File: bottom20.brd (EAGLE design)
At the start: 160 x 140 mm, 142 parts, among them T1:IC1 MULTIPLEXER, T1:R1 20k, T1:R10 20k, T1:R11 20k, T1:R12 20k, T1:R13 20k, T1:R14 20k, T1:R15 20k, T1:R16 20k, T1:R17 10k, T1:R2 20k, T1:R3 20k, T1:R4 20k, T1:R5 20k, T1:R6 20k, T1:R7 20k, T1:R8 20k, T1:R9 20k, T1:T1 SFH320, T1:T10 SFH320, T1:T11 SFH320, T1:T12 SFH320, T1:T13 SFH320, T1:T14 SFH320, T1:T15 SFH320, T1:T16 SFH320, T1:T2 SFH320, T1:T3 SFH320, T1:T4 SFH320, T1:T5 SFH320, T1:T6 SFH320, T1:T7 SFH320, T1:T8 SFH320, T1:T9 SFH320, T2:IC1 MULTIPLEXER, T2:R1 20k, T2:R10 20k, T2:R11 20k, T2:R12 20k, T2:R13 20k, T2:R14 20k, T2:R15 20k, T2:R16 20k, T2:R17 10k, T2:R2 20k, T2:R3 20k, T2:R4 20k, T2:R5 20k, T2:R6 20k, T2:R7 20k, T2:R8 20k, T2:R9 20k, T2:T1 SFH320, T2:T10 SFH320, T2:T11 SFH320, T2:T12 SFH320, T2:T13 SFH320, T2:T14 SFH320, T2:T15 SFH320, T2:T16 SFH320, T2:T2 SFH320, T2:T3 SFH320, T2:T4 SFH320, T2:T5 SFH320, T2:T6 SFH320, T2:T7 SFH320, T2:T8 SFH320, T2:T9 SFH320

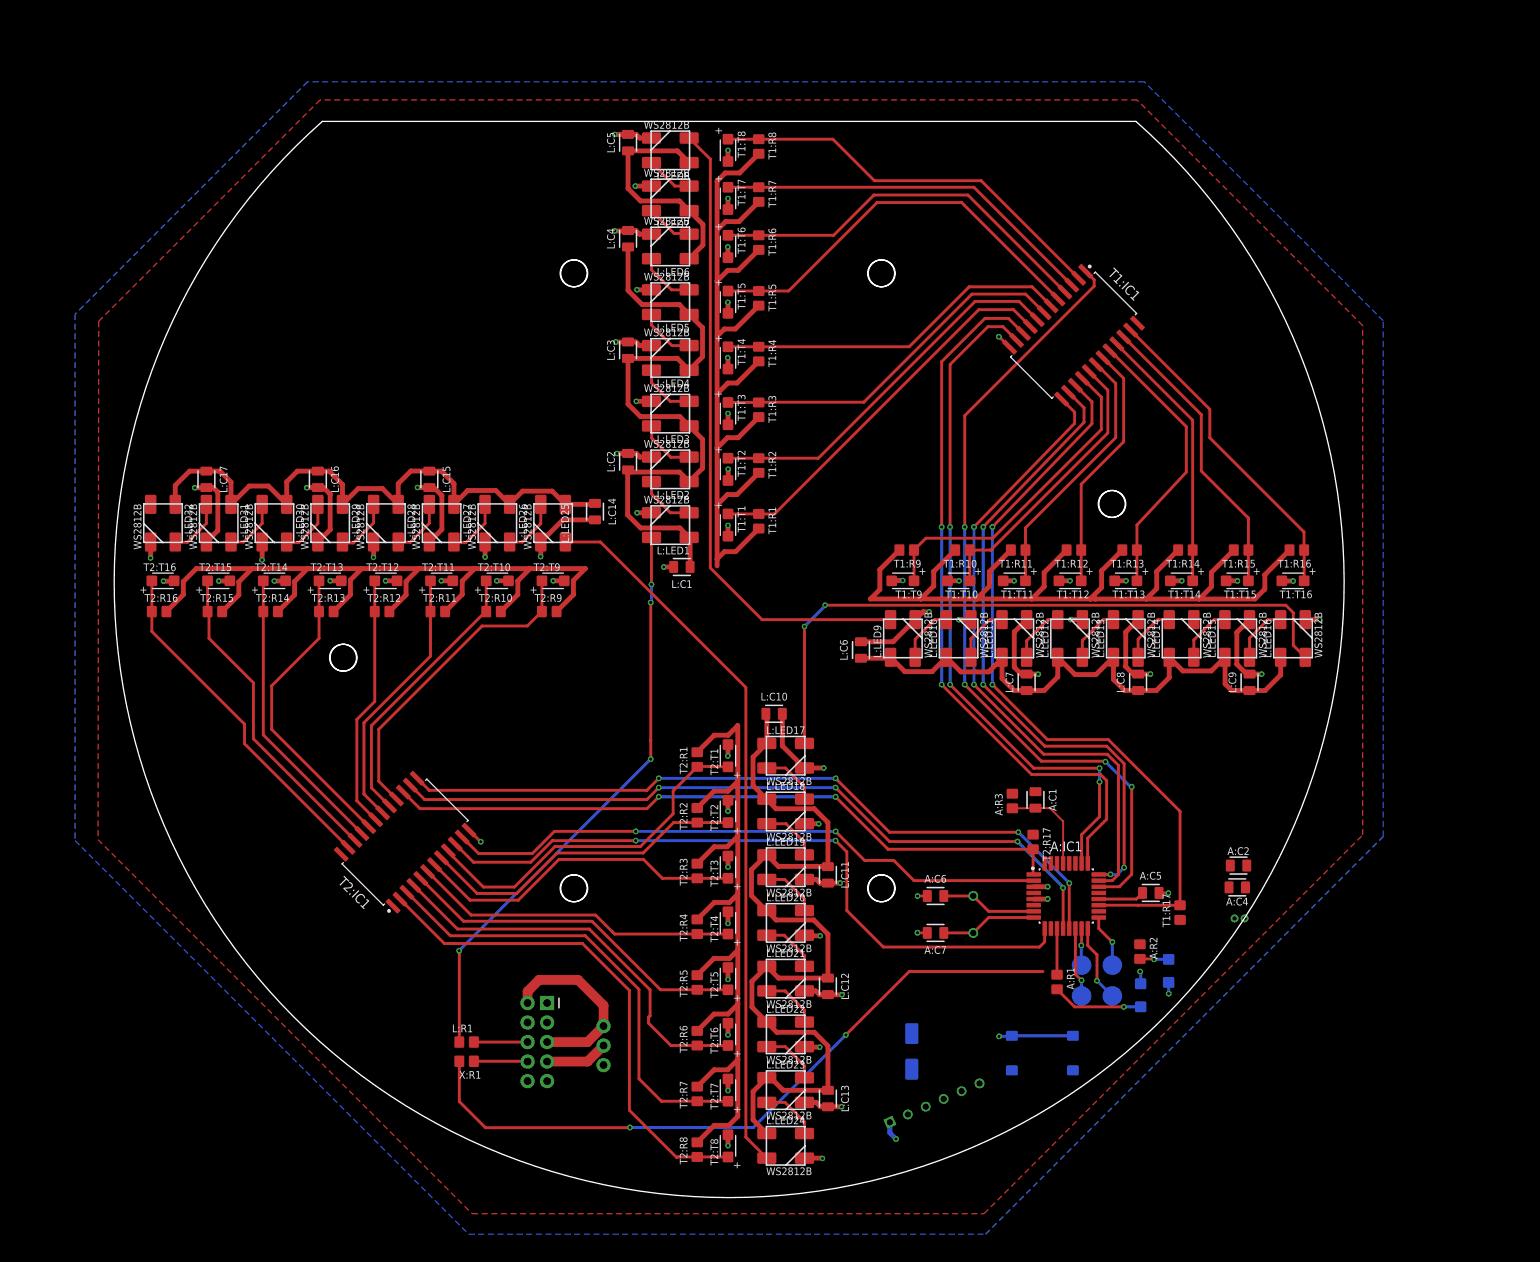
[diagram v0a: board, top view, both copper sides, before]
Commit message: - bot.sch (Routing - only 5V missing)
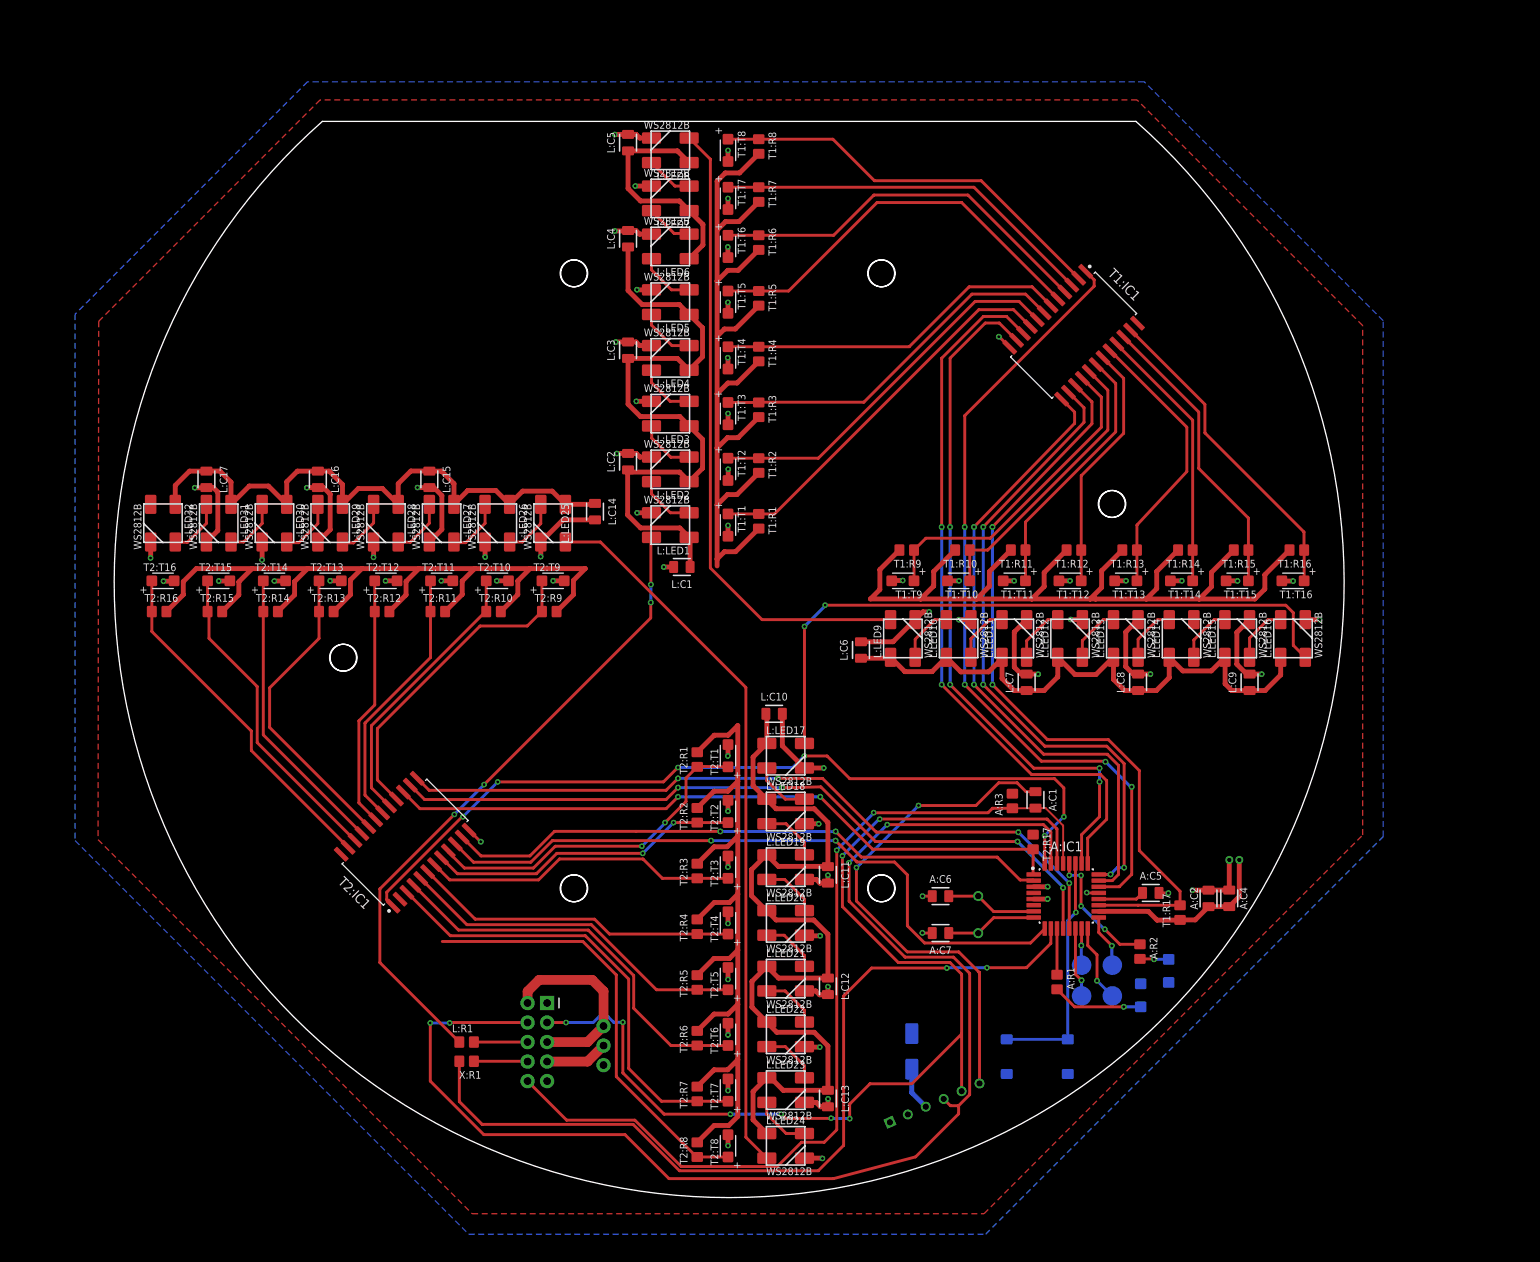
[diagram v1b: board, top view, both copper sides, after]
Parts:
- moved A:C3 7.64 mm to (65.9, -36.3), turned to 0 degrees
- moved A:C2 5.79 mm to (62.5, -41.3), turned to 90 degrees
- moved A:C4 1.77 mm to (65.2, -41.3), turned to 90 degrees
- moved A:S2 0.81 mm to (40.2, -61.9), turned to 180 degrees
- moved A:C7 0.65 mm to (27.6, -45.8)
- moved A:Q1 0.65 mm to (32.5, -43.4)
- moved A:C6 0.65 mm to (27.6, -41.0)
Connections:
- removed net A:ARD-INTERRUPT: A:IC1.10
- removed net X:ARD-INTERRUPT: X:R1.2
- removed net X:ARD-RX: X:X2.3
- removed net X:ARD-TX: X:X2.4
- new net ARD-INTERRUPT: A:IC1.10, X:R1.2
- net RX: now also X:X2.3
- net TX: now also X:X2.4
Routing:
- net TX: track 0.00 -> 175.5 mm, vias 0 -> 4
- net RX: track 0.00 -> 145.4 mm, vias 0 -> 8
- net ARD-INTERRUPT: track 0.00 -> 111.5 mm, vias 0 -> 2
- net N$2: track 0.00 -> 110.2 mm, vias 0 -> 6
- net ARD-RESET: track 12.8 -> 120.9 mm, vias 0 -> 2
- net X:ARD-INTERRUPT: track 91.0 -> 0.00 mm, vias 2 -> 0
- net DTR: track 0.00 -> 67.1 mm, vias 0 -> 2
- net A:N$9: track 0.00 -> 31.3 mm, vias 0 -> 1
- net +5V: track 824.3 -> 848.9 mm
- net A:N$11: track 0.00 -> 16.8 mm, vias 0 -> 4
- net T2:N$9: track 65.8 -> 56.5 mm
- net L:N$10: track 76.0 -> 84.6 mm
- net GND: track 241.3 -> 234.3 mm, vias 75 -> 73
- net X:VID: track 0.00 -> 5.64 mm
- net T2:N$2: track 43.0 -> 40.9 mm, vias 0 -> 2
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
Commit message: - bot.sch (Routing - corrections)
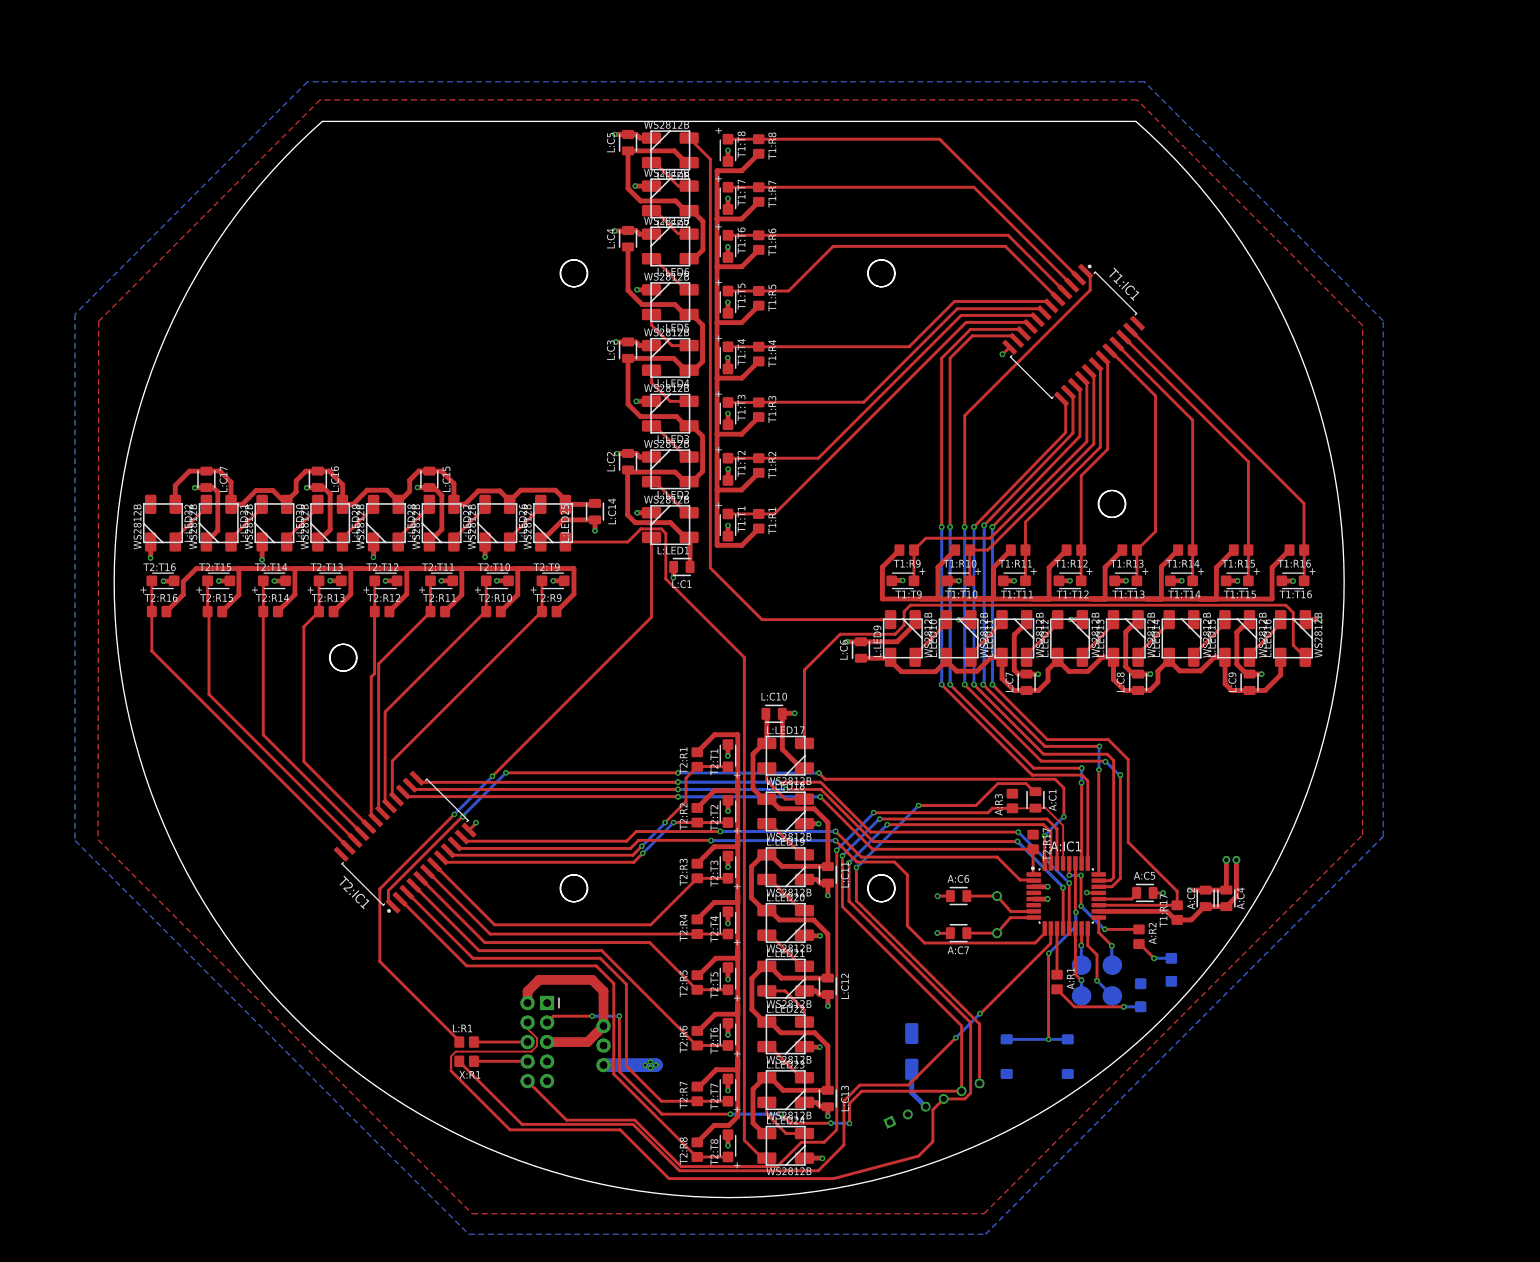
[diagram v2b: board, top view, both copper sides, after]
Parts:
- moved A:Q1 2.45 mm to (35.0, -43.4)
- moved A:C6 2.35 mm to (30.0, -41.0)
- moved A:C7 2.35 mm to (30.0, -45.8)
- moved A:R2 1.94 mm to (53.5, -46.3)
- moved A:C5 0.76 mm to (54.2, -40.6)
- moved A:C3 0.37 mm to (65.5, -36.3)
- moved A:C4 0.37 mm to (64.8, -41.3)
- moved T1:R17 0.37 mm to (58.4, -43.2)
- moved A:C2 0.37 mm to (62.1, -41.3)
- moved A:LED2 0.37 mm to (57.7, -50.6)
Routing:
- net +5V: track 848.9 -> 863.5 mm, vias 0 -> 4
- net ARD-INTERRUPT: track 111.5 -> 100.4 mm
- net TX: track 175.5 -> 166.1 mm, vias 4 -> 2
- net GND: track 234.3 -> 226.8 mm
- net L:CON-3: track 93.7 -> 101.1 mm
- net T2:N$9: track 56.5 -> 63.5 mm
- net N$9: track 84.0 -> 78.1 mm
- net RX: track 145.4 -> 139.7 mm
- net T2:N$7: track 41.9 -> 36.7 mm
- net N$10: track 94.7 -> 89.8 mm
- net T1:N$5: track 52.9 -> 48.2 mm
- net N$11: track 91.2 -> 86.6 mm
- net T1:N$11: track 51.2 -> 46.9 mm
- net DTR: track 67.1 -> 63.0 mm
- net T2:N$18: track 40.0 -> 36.3 mm
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
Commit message: - bot.sch (Routing - 5V Plane adjustments)
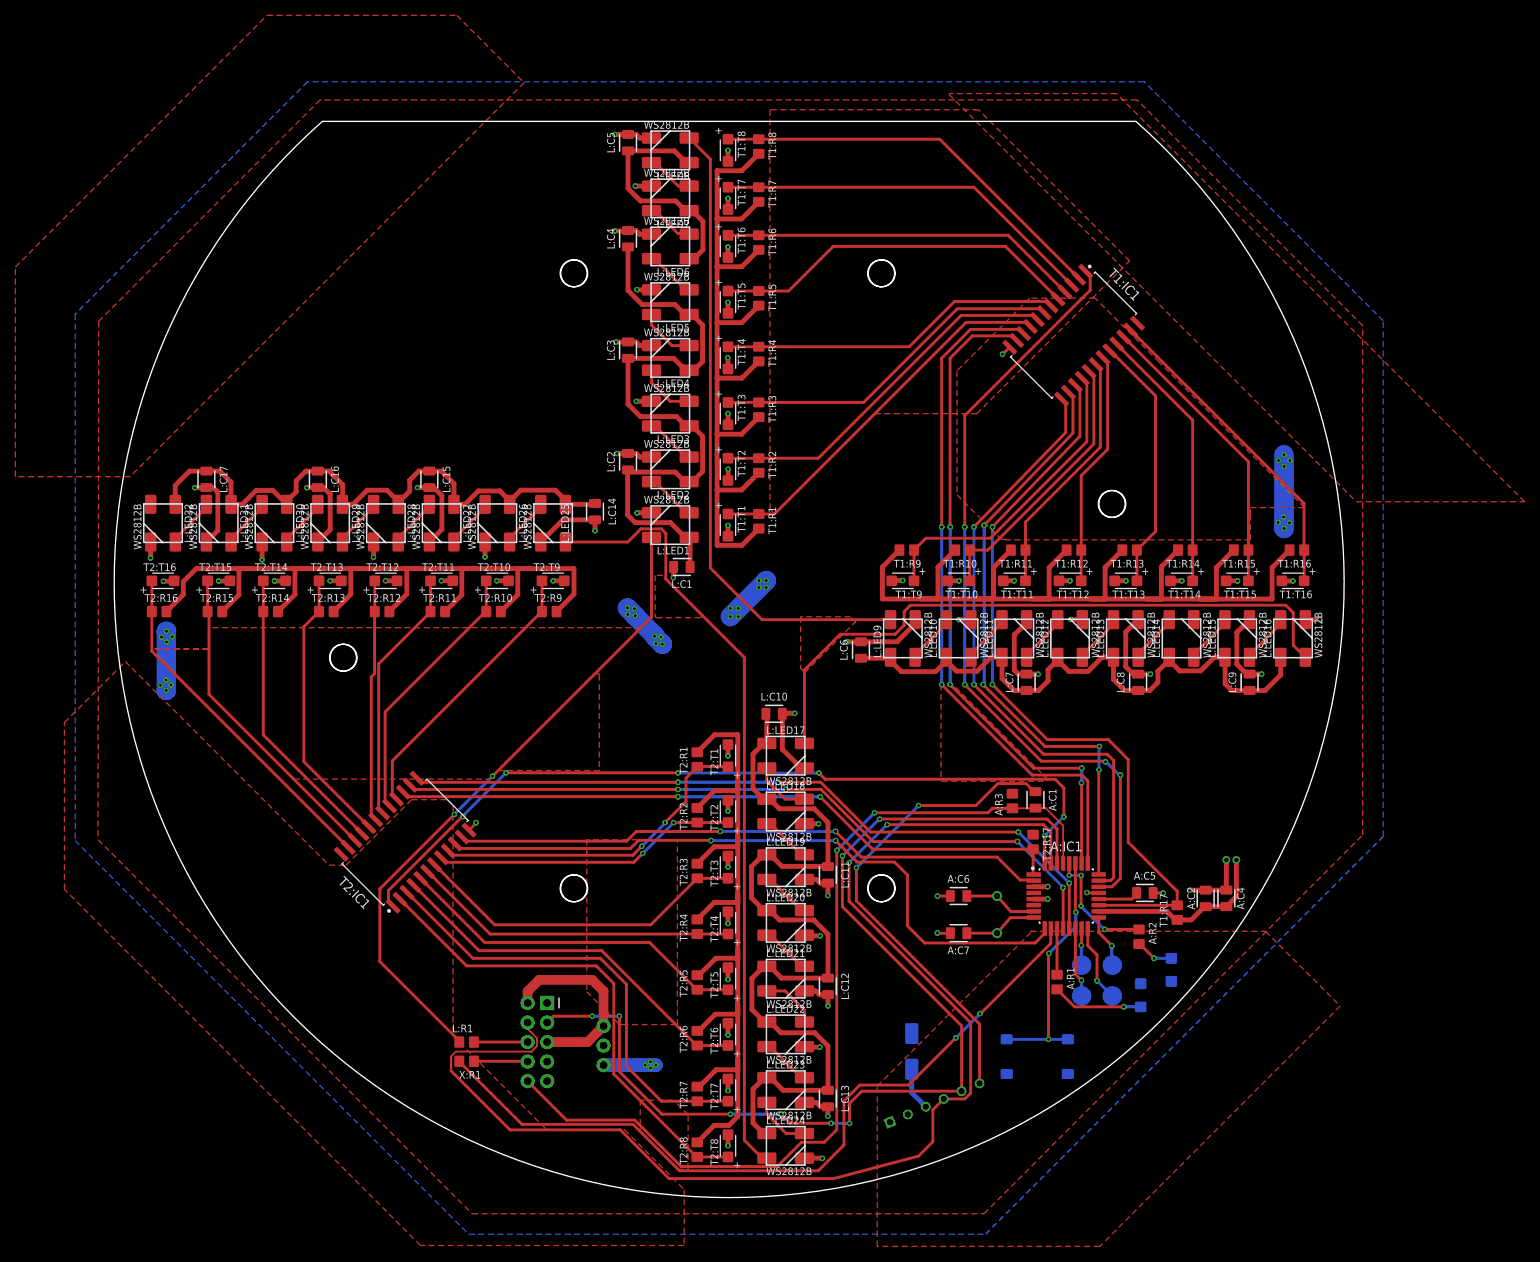
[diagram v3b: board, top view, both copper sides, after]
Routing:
- net +5V: track 863.5 -> 918.0 mm, vias 4 -> 36
- net T1:N$14: track 33.1 -> 32.5 mm

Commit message: - bot.brd (final changes)
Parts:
- moved A:C3 21.7 mm to (54.1, -54.8), turned to 180 degrees
- moved A:C4 11.9 mm to (55.4, -48.5), turned to 0 degrees
- moved A:LED2 10.3 mm to (50.6, -58.1)
- moved A:LED1 9.78 mm to (46.4, -60.4), turned to 270 degrees
- moved A:C2 8.09 mm to (55.4, -45.8), turned to 0 degrees
- moved A:TP2 1.87 mm to (48.2, -54.5)
- moved A:R2 1.74 mm to (51.7, -46.3)
- moved A:TP1 1.12 mm to (49.0, -50.5)
- moved A:TP4 0.86 mm to (45.3, -54.5)
- moved A:TP3 0.50 mm to (46.0, -50.5)
- moved A:R1 0.08 mm to (42.8, -52.3)
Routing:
- net +5V: track 918.0 -> 1026.3 mm, vias 36 -> 51
- net GND: track 226.8 -> 242.3 mm, vias 73 -> 76
- net A:N$10: track 4.98 -> 9.77 mm
- net A:N$4: track 11.8 -> 7.20 mm
- net N$6: track 95.8 -> 93.6 mm
- net N$7: track 96.4 -> 94.2 mm
- net TX: track 166.1 -> 164.2 mm
- net A:N$11: track 15.9 -> 14.1 mm
- net A:MOSI: track 4.80 -> 5.59 mm
- net RX: track 139.6 -> 140.3 mm
- net T1:N$20: track 34.4 -> 34.9 mm
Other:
- board text added: "2020"
- board text added: "Bottom"
- board text added: "Iceberg Robots"
- board text added: "Oona Kintscher"
- board text added: "designed by"
- board text added: "www.iceberg-robots.de"

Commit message: - brd (Labeling)
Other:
- board text added: "Design by Oona"
- board text removed: "Oona Kintscher"
- board text removed: "designed by"

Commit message: - bot.brd (Corrections)
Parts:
- moved L:C17 1.03 mm to (-67.6, 14.2)
- moved L:C15 1.00 mm to (-38.9, 14.2)
- moved L:C16 1.00 mm to (-53.4, 14.2)
- moved L:C7 1.00 mm to (38.9, -14.2)
- moved L:C8 1.00 mm to (53.4, -14.2)
- moved L:C9 1.00 mm to (67.8, -14.2)
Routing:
- net +5V: track 1026.3 -> 1033.1 mm
- net GND: track 242.3 -> 247.9 mm
- net ARD-INTERRUPT: track 100.4 -> 96.7 mm
- net RX: track 140.3 -> 138.5 mm

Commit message: - bot (Corrections 2.0)
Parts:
- added T1:C1, T2:C1: 100nF, iceberg20:C0805
- A:R1, A:R2: value 110 -> 110R
- L:R1, X:R1: value 330 -> 330R
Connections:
- removed net X:+5V: X:D1.1
- net +5V: now also T1:C1.1, T2:C1.1, X:D1.1
- net GND: now also T1:C1.2, T2:C1.2
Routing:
- net +5V: track 1033.1 -> 1068.9 mm, vias 51 -> 52
- net GND: track 247.9 -> 251.3 mm, vias 76 -> 78
